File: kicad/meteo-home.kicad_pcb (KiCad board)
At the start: 2 copper layers, 37.5 x 51.4 mm, 10 parts

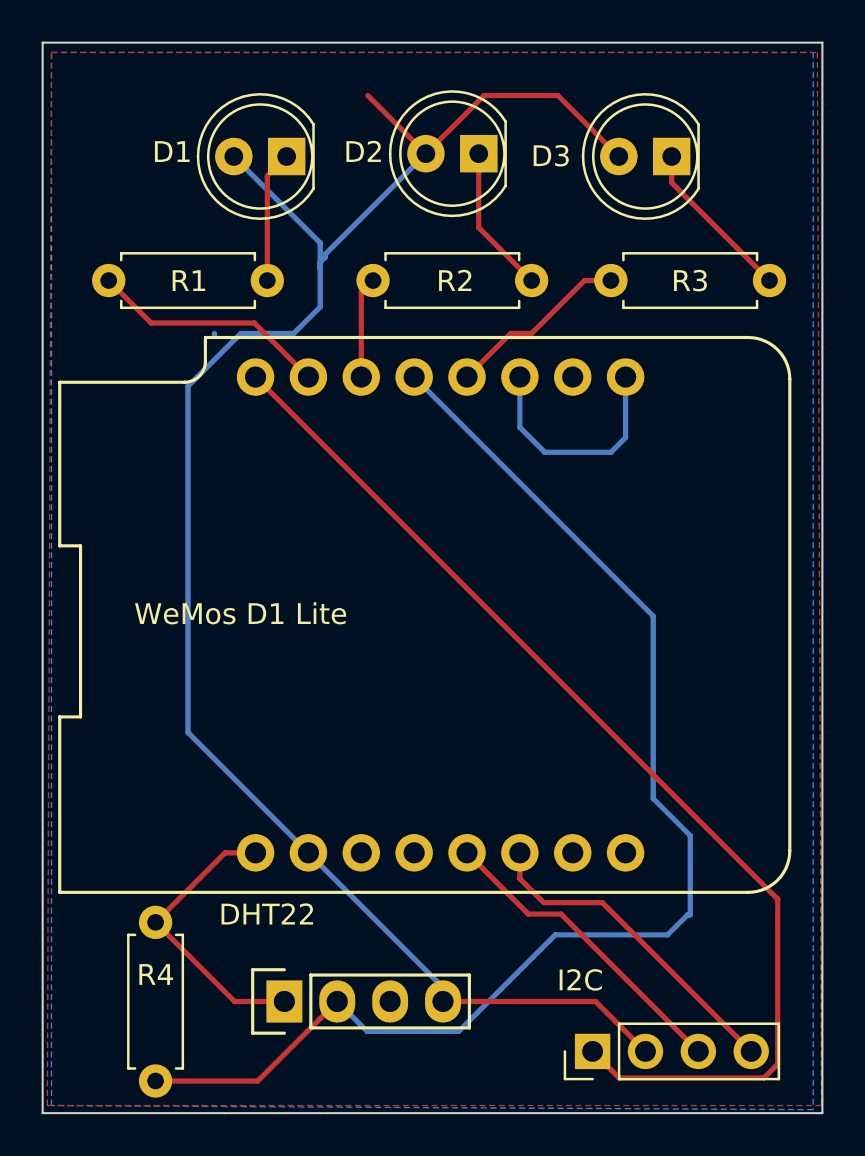
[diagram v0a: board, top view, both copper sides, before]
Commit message: Feat: i2c connectors pins and disposition changed
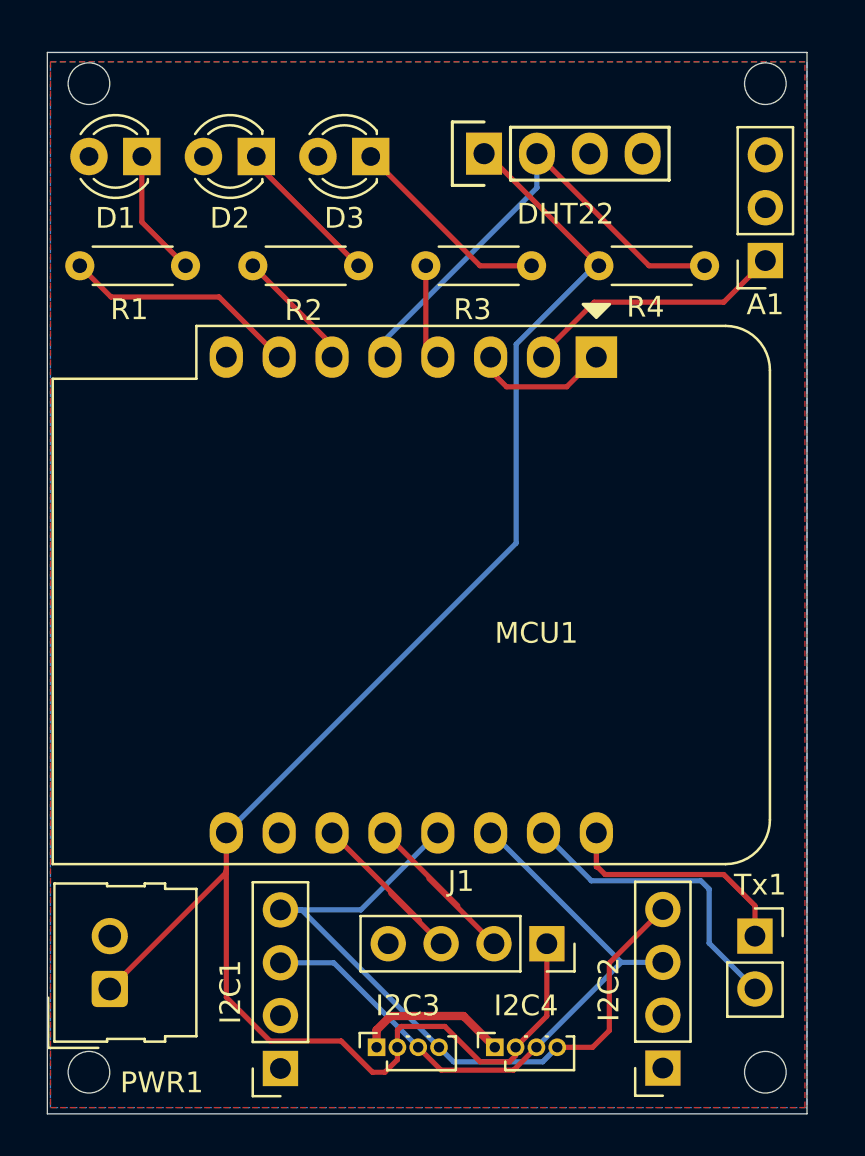
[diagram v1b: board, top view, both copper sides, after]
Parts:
- removed I2C: SGP30, Pin_Headers:Pin_Header_Straight_1x04_Pitch2.54mm
- added A1: Analog Sensor, Connector_PinSocket_2.54mm:PinSocket_1x03_P2.54mm_Vertical, F.Cu at (139.5, 60.0)
- added I2C1: I2C 1, Connector_PinSocket_2.54mm:PinSocket_1x04_P2.54mm_Vertical, F.Cu at (116.2, 98.8)
- added I2C2: I2C 2, Connector_PinSocket_2.54mm:PinSocket_1x04_P2.54mm_Vertical, F.Cu at (134.6, 98.8)
- added I2C3: I2C 3, Connector_PinSocket_1.00mm:PinSocket_1x04_P1.00mm_Vertical, F.Cu at (120.8, 97.8)
- added I2C4: I2C 4, Connector_PinSocket_1.00mm:PinSocket_1x04_P1.00mm_Vertical, F.Cu at (126.5, 97.8)
- added J1: S 4, Connector_PinSocket_2.54mm:PinSocket_1x04_P2.54mm_Vertical, F.Cu at (129.0, 92.8)
- added PWR1: Power connector, Connector_Molex:Molex_SL_171971-0002_1x02_P2.54mm_Vertical, F.Cu at (108.0, 95.0)
- added Tx1: Rx, Connector_PinSocket_2.54mm:PinSocket_1x02_P2.54mm_Vertical, F.Cu at (139.0, 92.5)
- D1, D2, D3: footprint LEDs:LED_D5.0mm -> LED_THT:LED_D3.0mm
- DHT22: value DHT22 -> DHT22_Temperature_Humidity
- MCU1: renamed from WeMos D1 Lite; footprint wemos-d1-mini:wemos-d1-mini-with-pin-header -> Module:WEMOS_D1_mini_light
- R1, R2, R3, R4: footprint Resistors_THT:R_Axial_DIN0207_L6.3mm_D2.5mm_P7.62mm_Horizontal -> Resistor_THT:R_Axial_DIN0204_L3.6mm_D1.6mm_P5.08mm_Horizontal
- moved DHT22 41.9 mm to (129.8, 54.9)
- moved R4 38.1 mm to (131.5, 60.2), turned to 0 degrees
- moved MCU1 14.5 mm to (131.4, 64.6), turned to -90 degrees
- moved D3 14.5 mm to (120.5, 55.0)
- moved R3 11.5 mm to (128.3, 60.2)
- moved D2 10.7 mm to (115.0, 55.0)
- moved R2 8.35 mm to (120.0, 60.2)
- moved D1 6.96 mm to (109.5, 55.0)
- moved R1 3.99 mm to (111.6, 60.2)
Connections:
- net /5V renamed VCC
- net /GND renamed GND
- DHT22 pad 3: (no net) -> unconnected-(DHT22-NULL-Pad3)
- MCU1 pad 11: (no net) -> Net-(J1-Pin_3)
- MCU1 pad 12: (no net) -> Net-(J1-Pin_2)
- MCU1 pad 13: Net-(U1-Pad13) -> SDA
- MCU1 pad 14: Net-(U1-Pad14) -> SCL
- MCU1 pad 15: (no net) -> Net-(MCU1-Rx)
- MCU1 pad 16: (no net) -> Net-(MCU1-Tx)
- MCU1 pad 2: (no net) -> A0
- MCU1 pad 8: /3.3V -> +3V3
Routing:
- net GND: track 85.9 -> 7.41 mm
- net VCC: track 14.0 -> 82.7 mm
- net /3.3V: track 53.1 -> 0.00 mm
- net Net-(DHT22-DATA): track 61.5 -> 23.1 mm
- net SDA: track 0.00 -> 35.4 mm
- net SCL: track 0.00 -> 31.5 mm
- net Net-(U1-Pad14): track 15.8 -> 0.00 mm
- net Net-(U1-Pad13): track 15.1 -> 0.00 mm
- net Net-(MCU1-Rx): track 0.00 -> 14.8 mm
- net A0: track 0.00 -> 12.7 mm
- net Net-(MCU1-Tx): track 0.00 -> 11.5 mm
- net Net-(J1-Pin_3): track 0.00 -> 9.37 mm
- net Net-(J1-Pin_2): track 0.00 -> 9.37 mm
- net Net-(MCU1-D0): track 11.2 -> 6.65 mm
- net Net-(MCU1-D5): track 8.84 -> 4.63 mm
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- added copper zone on B.Cu, net +3V3
- removed copper zone on B.Cu, net GND
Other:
- board size 37.5 x 51.4 mm -> 36.5 x 51 mm
- board text added: "3v3"
- board text added: "5V"
- board text added: "A0"
- board text added: "D3"
- board text added: "D4"
- board text added: "MeteoHome Rev 2.0 https://github.com/deuteros76/meteo-home"
- board text added: "RX"
- board text added: "TX"
- board text removed: "MeteoHome Rev 3 https://github.com/deuteros76/meteo-home"

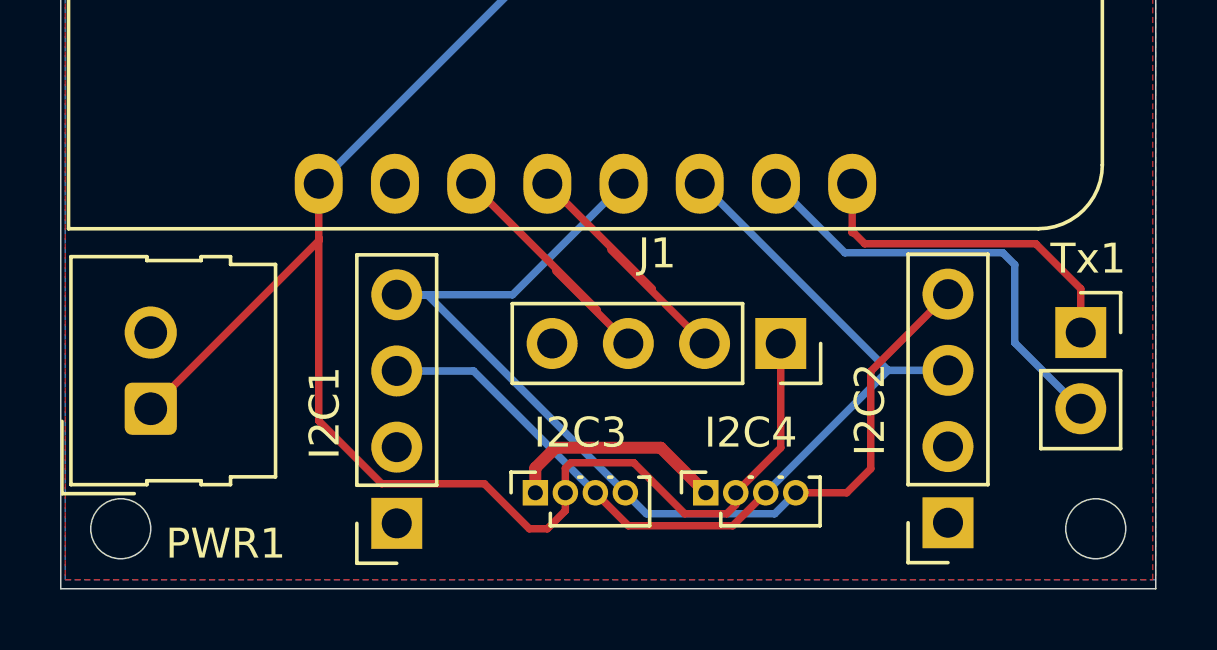
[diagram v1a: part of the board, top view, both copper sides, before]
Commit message: Fix: connectors relocation
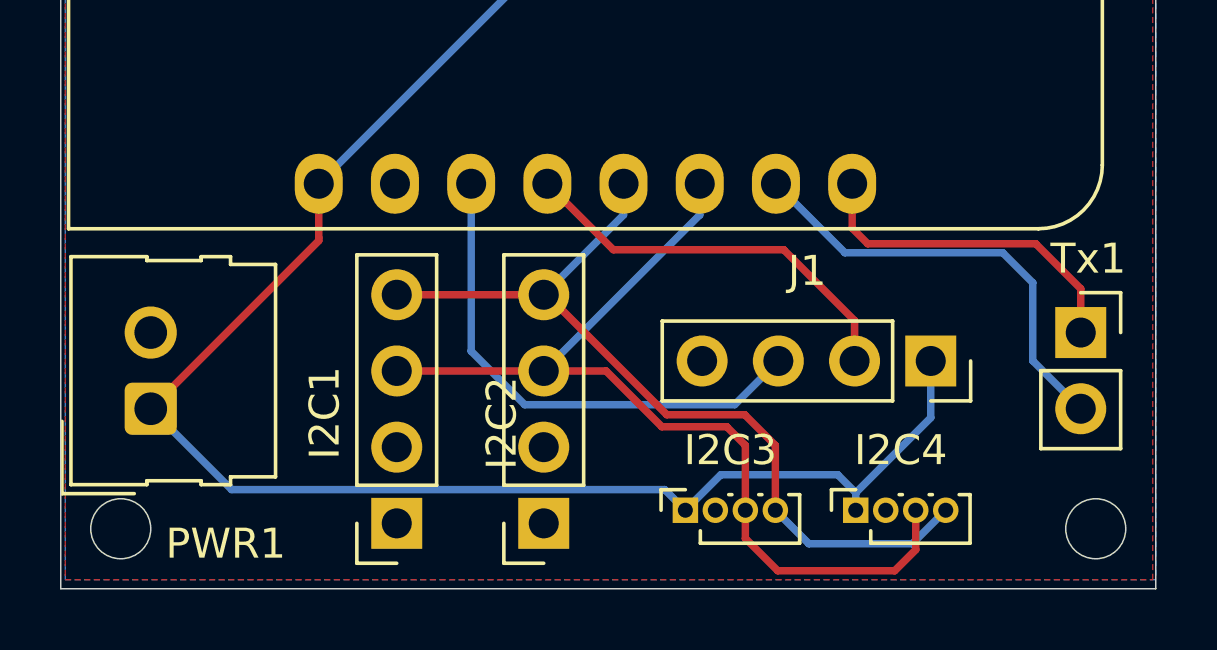
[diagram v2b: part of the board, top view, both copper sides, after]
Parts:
- moved I2C2 13.5 mm to (121.1, 98.8)
- moved I2C3 5.03 mm to (125.8, 98.4)
- moved I2C4 5.03 mm to (131.5, 98.4)
- moved J1 5.03 mm to (134.0, 93.4)
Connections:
- I2C1 pad 1: GND -> +3V3
- I2C1 pad 2: +3V3 -> GND
- I2C2 pad 1: GND -> +3V3
- I2C2 pad 2: +3V3 -> GND
- I2C3 pad 1: GND -> VCC
- I2C3 pad 2: VCC -> GND
- I2C4 pad 1: GND -> VCC
- I2C4 pad 2: VCC -> GND
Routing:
- net Net-(J1-Pin_3): track 9.37 -> 17.2 mm
- net GND: track 7.41 -> 0.00 mm
- net SDA: track 35.4 -> 28.8 mm
- net Net-(J1-Pin_2): track 9.37 -> 13.5 mm
- net VCC: track 82.7 -> 84.3 mm
